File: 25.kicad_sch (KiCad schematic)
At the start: 22 parts, among them J23 HDR_2X3, J24 CON_MUSB-AB_5_F, U23 AM6442BSFGHAALV, U36 TPS2051BD, U38 TPD4S012DRYR

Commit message: fix joint, offpage, and typo
DRC errors are cleared, some warnings remain.
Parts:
- removed *: MISTRAL_TITLEBLK_CSIZE, symbol 25-altium-import:root_0_MISTRAL_TITLEBLK_CSIZE
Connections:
- net DGND: now also C153.1
- net USB0_AB_DM: now also U38.1 (D+)
- net USB0_AB_DP: now also U38.2 (D-)
- net USB0_AB_ID: now also U38.3 (ID)
- net USB0_DRVBUS: now also R151.1
- net USB0_RCALIB: now also R605.1
- net USB0_VBUS: now also C140.1, J24.1 (VCC), U36.6 (OUT1), U36.7 (OUT2), U36.8 (OUT3), U38.6 (VBUS)
- net USB1_SHIELD: now also C153.2, J24.10 (SH5), J24.6 (SH1), J24.8 (SH3)
- net VCC_5V0: now also FL7.1 (INPUT)
- net at U36.2 (IN1): now also C141.1, FL7.3 (OUTPUT), U36.3 (IN2)
- net at R427.1, R428.2: now also D7.3 (C)

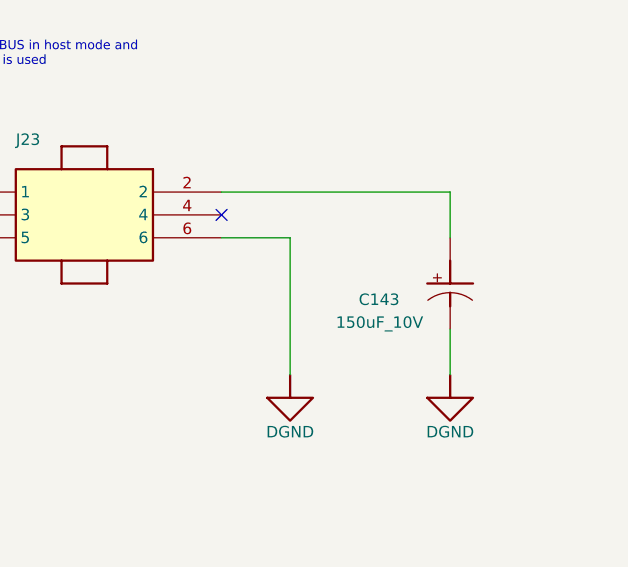
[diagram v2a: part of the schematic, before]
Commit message: fixpcb.
TODO clean up zones and keepouts on all layers. (top done almost)
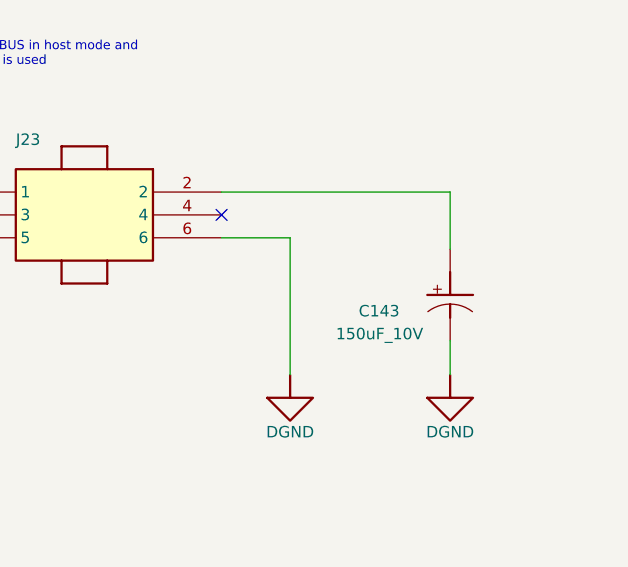
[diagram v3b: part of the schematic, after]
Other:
- moved on the sheet: C143
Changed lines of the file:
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@@
 	(wire
 		(pts
-			(xy 464.82 109.22) (xy 464.82 104.14)
+			(xy 464.82 109.22) (xy 464.82 105.41)
 		)
 		(stroke
@@
 	(wire
 		(pts
-			(xy 464.82 93.98) (xy 464.82 88.9)
+			(xy 464.82 95.25) (xy 464.82 88.9)
 		)
 		(stroke
@@
 	(symbol
 		(lib_id "25-altium-import:root_0_mirrored_CAP_POL_Dup1")
-		(at 467.36 96.52 0)
+		(at 467.36 97.79 0)
 		(unit 1)
 		(exclude_from_sim no)
@@
 		(dnp no)
 		(property "Reference" "C143"
-			(at 454.66 101.6 0)
+			(at 454.66 102.87 0)
 			(effects
 				(font
@@
 		)
 		(property "Value" "150uF_10V"
-			(at 452.12 104.14 0)
+			(at 452.12 105.41 0)
 			(effects
 				(font
@@
 		)
 		(property "Footprint" "CAPT7343D_3-25"
-			(at 467.36 96.52 0)
+			(at 467.36 97.79 0)
 			(effects
 				(font
@@
 		)
 		(property "Datasheet" ""
-			(at 467.36 96.52 0)
+			(at 467.36 97.79 0)
 			(effects
 				(font
@@
 		)
 		(property "Description" "CAP TANTALUM 150uF 10V 10% ESR 0.9E D7343"
-			(at 467.36 96.52 0)
+			(at 467.36 97.79 0)
 			(effects
 				(font
@@
 		)
 		(property "FOOTPRINT PATH" "Y~{:}MIS_DATABAS~{E}Librar~{y}ALTIUM_TOO~{L}PCB_FOOTPRINT~{S}Altium_Footprint_Lib.PcbLib"
-			(at 5.08 386.08 0)
+			(at 5.08 387.35 0)
 			(effects
 				(font
@@
 		)
 		(property "LIBRARY PATH" "Y~{:}MIS_DATABAS~{E}Librar~{y}ALTIUM_TOO~{L}SCHEMATICS_PART~{S}MS_DISCRETE_Library.schlib"
-			(at 5.08 386.08 0)
+			(at 5.08 387.35 0)
 			(effects
 				(font
@@
 		)
 		(property "FOOTPRINT REF" "CAPT7343D_3-25"
-			(at 5.08 386.08 0)
+			(at 5.08 387.35 0)
 			(effects
 				(font
@@
 		)
 		(property "MECHANICAL 3D STEP FILE" "CAPT7343D_3-25"
-			(at 5.08 386.08 0)
+			(at 5.08 387.35 0)
 			(effects
 				(font
@@
 		)
 		(property "CUSTOM_DUTY" "15%"
-			(at 5.08 386.08 0)
+			(at 5.08 387.35 0)
 			(effects
 				(font
@@
 		)
 		(property "CUSTOMS_HS_CODE" "85322990"
-			(at 5.08 386.08 0)
+			(at 5.08 387.35 0)
 			(effects
 				(font
@@
 		)
 		(property "ROHS" ""
-			(at 5.08 386.08 0)
+			(at 5.08 387.35 0)
 			(effects
 				(font
@@
 		)
 		(property "CHKD/DATE" "MANIRAJA/240118"
-			(at 5.08 386.08 0)
+			(at 5.08 387.35 0)
 			(effects
 				(font
@@
 		)
 		(property "CRTD /DATE" "MANIRAJA/240118"
-			(at 5.08 386.08 0)
+			(at 5.08 387.35 0)
 			(effects
 				(font
@@
 		)
 		(property "DATASHEET" "Y~{:}MIS_DATABAS~{E}DATASHEET~{S}CAPACITOR~{S}AVX-TAJ-SER.PDF"
-			(at 5.08 386.08 0)
+			(at 5.08 387.35 0)
 			(effects
 				(font
@@
 		)
 		(property "TEMPERATURE" "-55癈+125癈"
-			(at 5.08 386.08 0)
+			(at 5.08 387.35 0)
 			(effects
 				(font
@@
 		)
 		(property "WEIGHT" "670mg"
-			(at 5.08 386.08 0)
+			(at 5.08 387.35 0)
 			(effects
 				(font
@@
 		)
 		(property "HEIGHT" "3.10MM"
-			(at 5.08 386.08 0)
+			(at 5.08 387.35 0)
 			(effects
 				(font
@@
 		)
 		(property "DISTRIBUTOR_PART_NUMBER" "478-11241-1-ND"
-			(at 5.08 386.08 0)
+			(at 5.08 387.35 0)
 			(effects
 				(font
@@
 		)
 		(property "DISTRIBUTOR_NAME" "DIGIKEY"
-			(at 5.08 386.08 0)
+			(at 5.08 387.35 0)
 			(effects
 				(font
@@
 		)
 		(property "PACKAGE" "D7343"
-			(at 5.08 386.08 0)
+			(at 5.08 387.35 0)
 			(effects
 				(font
@@
 		)
 		(property "WATTAGE" "NA"
-			(at 5.08 386.08 0)
+			(at 5.08 387.35 0)
 			(effects
 				(font
@@
 		)
 		(property "VOLTAGE" "10V"
-			(at 5.08 386.08 0)
+			(at 5.08 387.35 0)
 			(effects
 				(font
@@
 		)
 		(property "TOLERANCE" "10%"
-			(at 5.08 386.08 0)
+			(at 5.08 387.35 0)
 			(effects
 				(font
@@
 		)
 		(property "PART_TYPE" "CAPACITOR~{S}TANTALUM"
-			(at 5.08 386.08 0)
+			(at 5.08 387.35 0)
 			(effects
 				(font
@@
 		)
 		(property "MFR_PART_NUMBER" "TAJD157K010TNJV"
-			(at 5.08 386.08 0)
+			(at 5.08 387.35 0)
 			(effects
 				(font
@@
 		)
 		(property "MFR_NAME" "AVX CORPORATION"
-			(at 5.08 386.08 0)
+			(at 5.08 387.35 0)
 			(effects
 				(font
@@
 		)
 		(property "PROJECT" "TI_MAXIE_CPB"
-			(at 5.08 386.08 0)
+			(at 5.08 387.35 0)
 			(effects
 				(font
@@
 		)
 		(property "MISTRAL PART NO" "120018010025-R"
-			(at 5.08 386.08 0)
+			(at 5.08 387.35 0)
 			(effects
 				(font
@@
 		)
 		(property "LIBRARY REF" "CAP_POL"
-			(at 5.08 386.08 0)
+			(at 5.08 387.35 0)
 			(effects
 				(font
@@
 		)
 		(property "PCB FOOTPRINT" "CAPT7343D_3-25"
-			(at 5.08 386.08 0)
-			(effects
-				(font
+			(at 5.08 387.35 0)
+			(effects
+				(font
